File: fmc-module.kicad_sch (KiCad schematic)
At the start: 0 parts

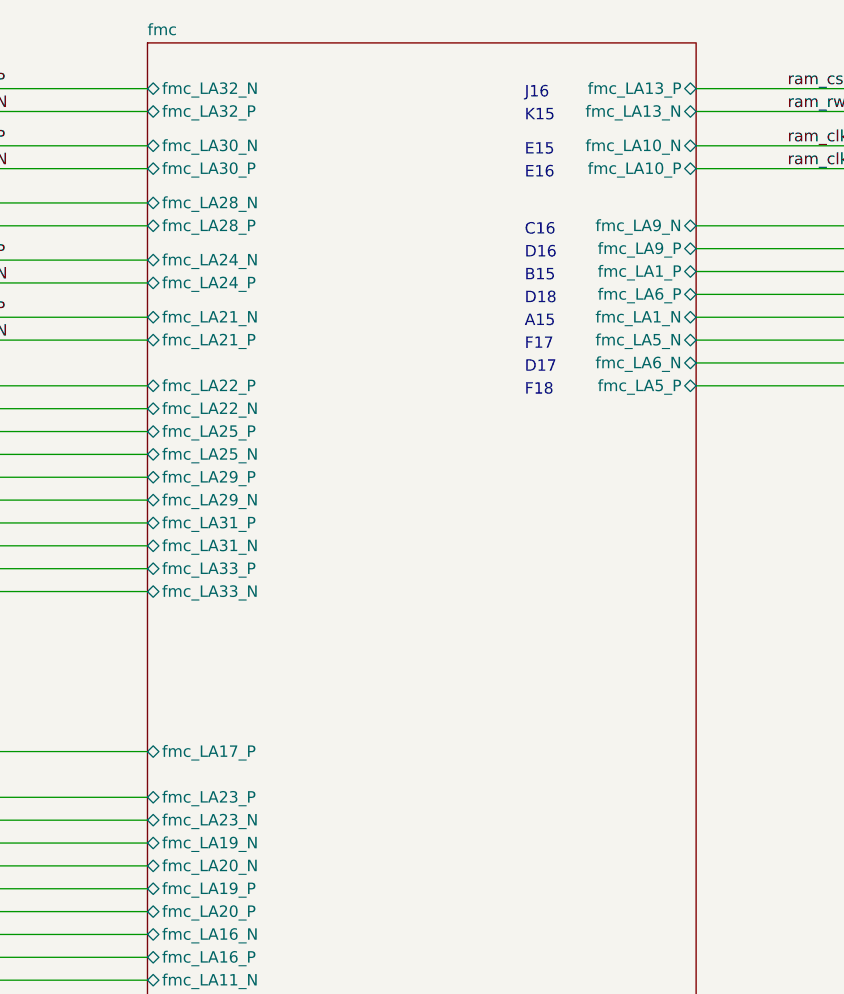
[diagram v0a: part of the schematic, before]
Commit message: Fixed wrong FMC pin labels
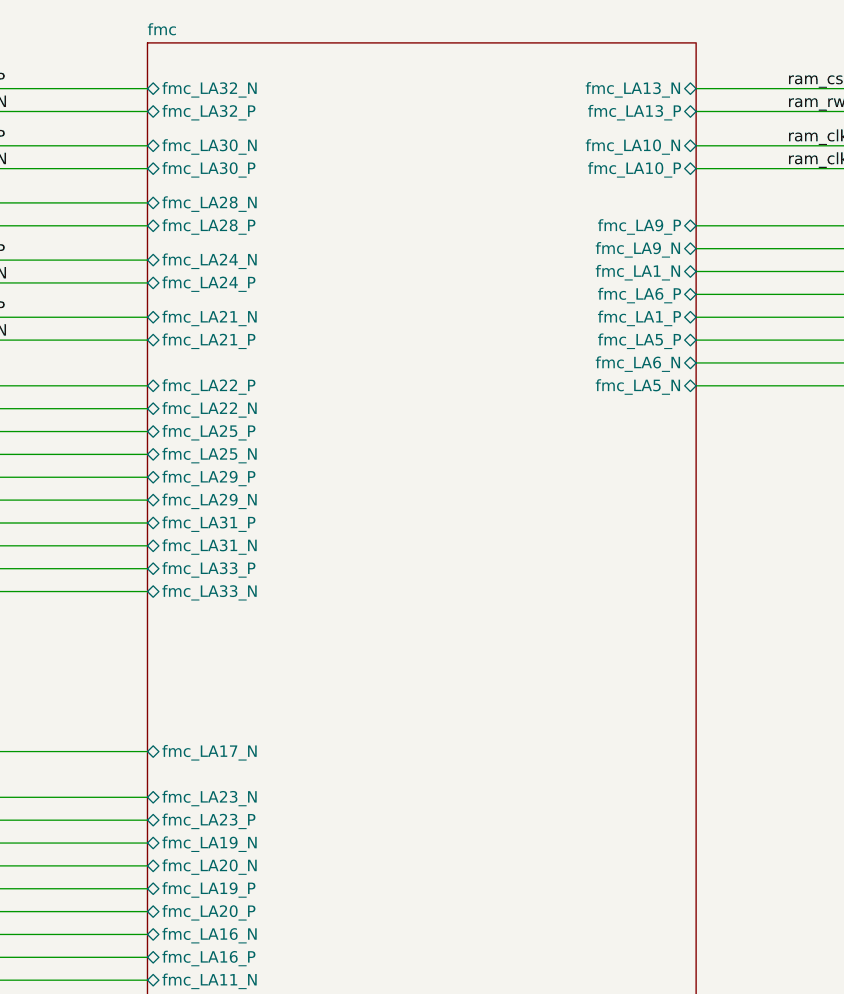
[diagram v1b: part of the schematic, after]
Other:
- sheet fmc ports: added fmc_LA17_N; removed fmc_LA17_P
- note removed: "A15"
- note removed: "B15"
- note removed: "C16"
- note removed: "D16"
- note removed: "D17"
- note removed: "D18"
- note removed: "E15"
- note removed: "E16"
- note removed: "F17"
- note removed: "F18"
- note removed: "J16"
- note removed: "K15"
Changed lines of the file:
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@@
 		(company "Konstantin Schauwecker")
-	)
-	(text "D17"
-		(exclude_from_sim no)
-		(at 142.24 55.88 0)
-		(effects
-			(font
-				(size 1.27 1.27)
-			)
-			(justify left bottom)
-		)
-	)
-	(text "K15"
-		(exclude_from_sim no)
-		(at 142.24 27.94 0)
-		(effects
-			(font
-				(size 1.27 1.27)
-			)
-			(justify left bottom)
-		)
-	)
-	(text "A15"
-		(exclude_from_sim no)
-		(at 142.24 50.8 0)
-		(effects
-			(font
-				(size 1.27 1.27)
-			)
-			(justify left bottom)
-		)
-	)
-	(text "C16"
-		(exclude_from_sim no)
-		(at 142.24 40.64 0)
-		(effects
-			(font
-				(size 1.27 1.27)
-			)
-			(justify left bottom)
-		)
-	)
-	(text "F17"
-		(exclude_from_sim no)
-		(at 142.24 53.34 0)
-		(effects
-			(font
-				(size 1.27 1.27)
-			)
-			(justify left bottom)
-		)
-	)
-	(text "E15"
-		(exclude_from_sim no)
-		(at 142.24 31.75 0)
-		(effects
-			(font
-				(size 1.27 1.27)
-			)
-			(justify left bottom)
-		)
-	)
-	(text "J16"
-		(exclude_from_sim no)
-		(at 142.24 25.4 0)
-		(effects
-			(font
-				(size 1.27 1.27)
-			)
-			(justify left bottom)
-		)
-	)
-	(text "B15"
-		(exclude_from_sim no)
-		(at 142.24 45.72 0)
-		(effects
-			(font
-				(size 1.27 1.27)
-			)
-			(justify left bottom)
-		)
-	)
-	(text "E16"
-		(exclude_from_sim no)
-		(at 142.24 34.29 0)
-		(effects
-			(font
-				(size 1.27 1.27)
-			)
-			(justify left bottom)
-		)
-	)
-	(text "F18"
-		(exclude_from_sim no)
-		(at 142.24 58.42 0)
-		(effects
-			(font
-				(size 1.27 1.27)
-			)
-			(justify left bottom)
-		)
-	)
-	(text "D16"
-		(exclude_from_sim no)
-		(at 142.24 43.18 0)
-		(effects
-			(font
-				(size 1.27 1.27)
-			)
-			(justify left bottom)
-		)
-	)
-	(text "D18"
-		(exclude_from_sim no)
-		(at 142.24 48.26 0)
-		(effects
-			(font
-				(size 1.27 1.27)
-			)
-			(justify left bottom)
-		)
 	)
 	(bus_entry
@@
 		)
 		(pin "fmc_LA23_N" bidirectional
+			(at 100.33 102.87 180)
+			(effects
+				(font
+					(size 1.27 1.27)
+				)
+				(justify left)
+			)
+		)
+		(pin "fmc_LA23_P" bidirectional
 			(at 100.33 105.41 180)
 			(effects
@@
 			)
 		)
-		(pin "fmc_LA23_P" bidirectional
-			(at 100.33 102.87 180)
-			(effects
-				(font
-					(size 1.27 1.27)
-				)
-				(justify left)
-			)
-		)
 		(pin "fmc_LA1_N" bidirectional
+			(at 161.29 44.45 0)
+			(effects
+				(font
+					(size 1.27 1.27)
+				)
+				(justify right)
+			)
+		)
+		(pin "fmc_LA1_P" bidirectional
 			(at 161.29 49.53 0)
-			(effects
-				(font
-					(size 1.27 1.27)
-				)
-				(justify right)
-			)
-		)
-		(pin "fmc_LA1_P" bidirectional
-			(at 161.29 44.45 0)
 			(effects
 				(font
@@
 		)
 		(pin "fmc_LA5_N" bidirectional
-			(at 161.29 52.07 0)
+			(at 161.29 57.15 0)
 			(effects
 				(font
@@
 		)
 		(pin "fmc_LA5_P" bidirectional
-			(at 161.29 57.15 0)
+			(at 161.29 52.07 0)
 			(effects
 				(font
@@
 		)
 		(pin "fmc_LA9_N" bidirectional
-			(at 161.29 39.37 0)
+			(at 161.29 41.91 0)
 			(effects
 				(font
@@
 		)
 		(pin "fmc_LA9_P" bidirectional
-			(at 161.29 41.91 0)
+			(at 161.29 39.37 0)
 			(effects
 				(font
@@
 		)
 		(pin "fmc_LA13_P" bidirectional
+			(at 161.29 26.67 0)
+			(effects
+				(font
+					(size 1.27 1.27)
+				)
+				(justify right)
+			)
+		)
+		(pin "fmc_LA13_N" bidirectional
 			(at 161.29 24.13 0)
-			(effects
-				(font
-					(size 1.27 1.27)
-				)
-				(justify right)
-			)
-		)
-		(pin "fmc_LA13_N" bidirectional
-			(at 161.29 26.67 0)
 			(effects
 				(font
@@
 			)
 		)
-		(pin "fmc_LA17_P" bidirectional
-			(at 100.33 97.79 180)
-			(effects
-				(font
-					(size 1.27 1.27)
-				)
-				(justify left)
-			)
-		)
 		(pin "fmc_LA18_P" bidirectional
 			(at 100.33 170.18 180)
 			(effects
 				(font
+					(size 1.27 1.27)
+				)
+				(justify left)
+			)
+		)
+		(pin "fmc_LA17_N" bidirectional
+			(at 100.33 97.79 180)
+			(effects
+				(font
